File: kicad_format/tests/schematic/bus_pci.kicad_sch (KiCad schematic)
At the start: 33 parts, among them U1 24C16, U11 S5933_PQ160

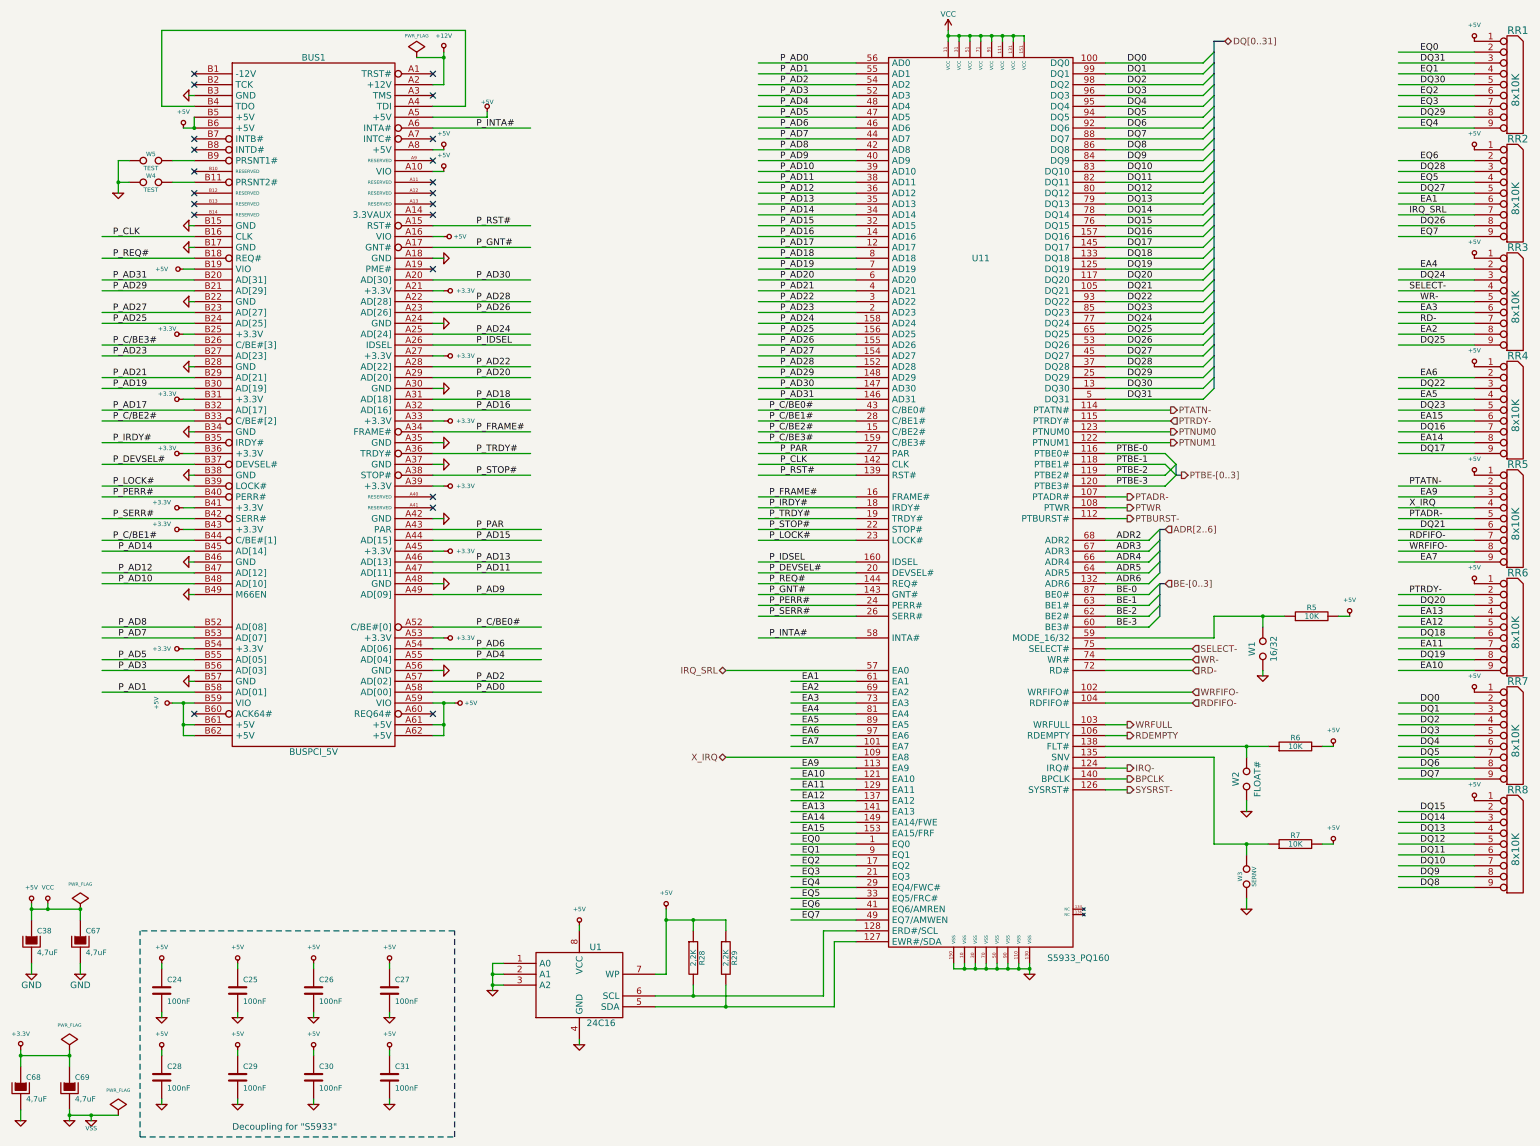
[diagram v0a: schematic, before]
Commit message: Add serialization context and support most modern kicad file idiosyncrasies
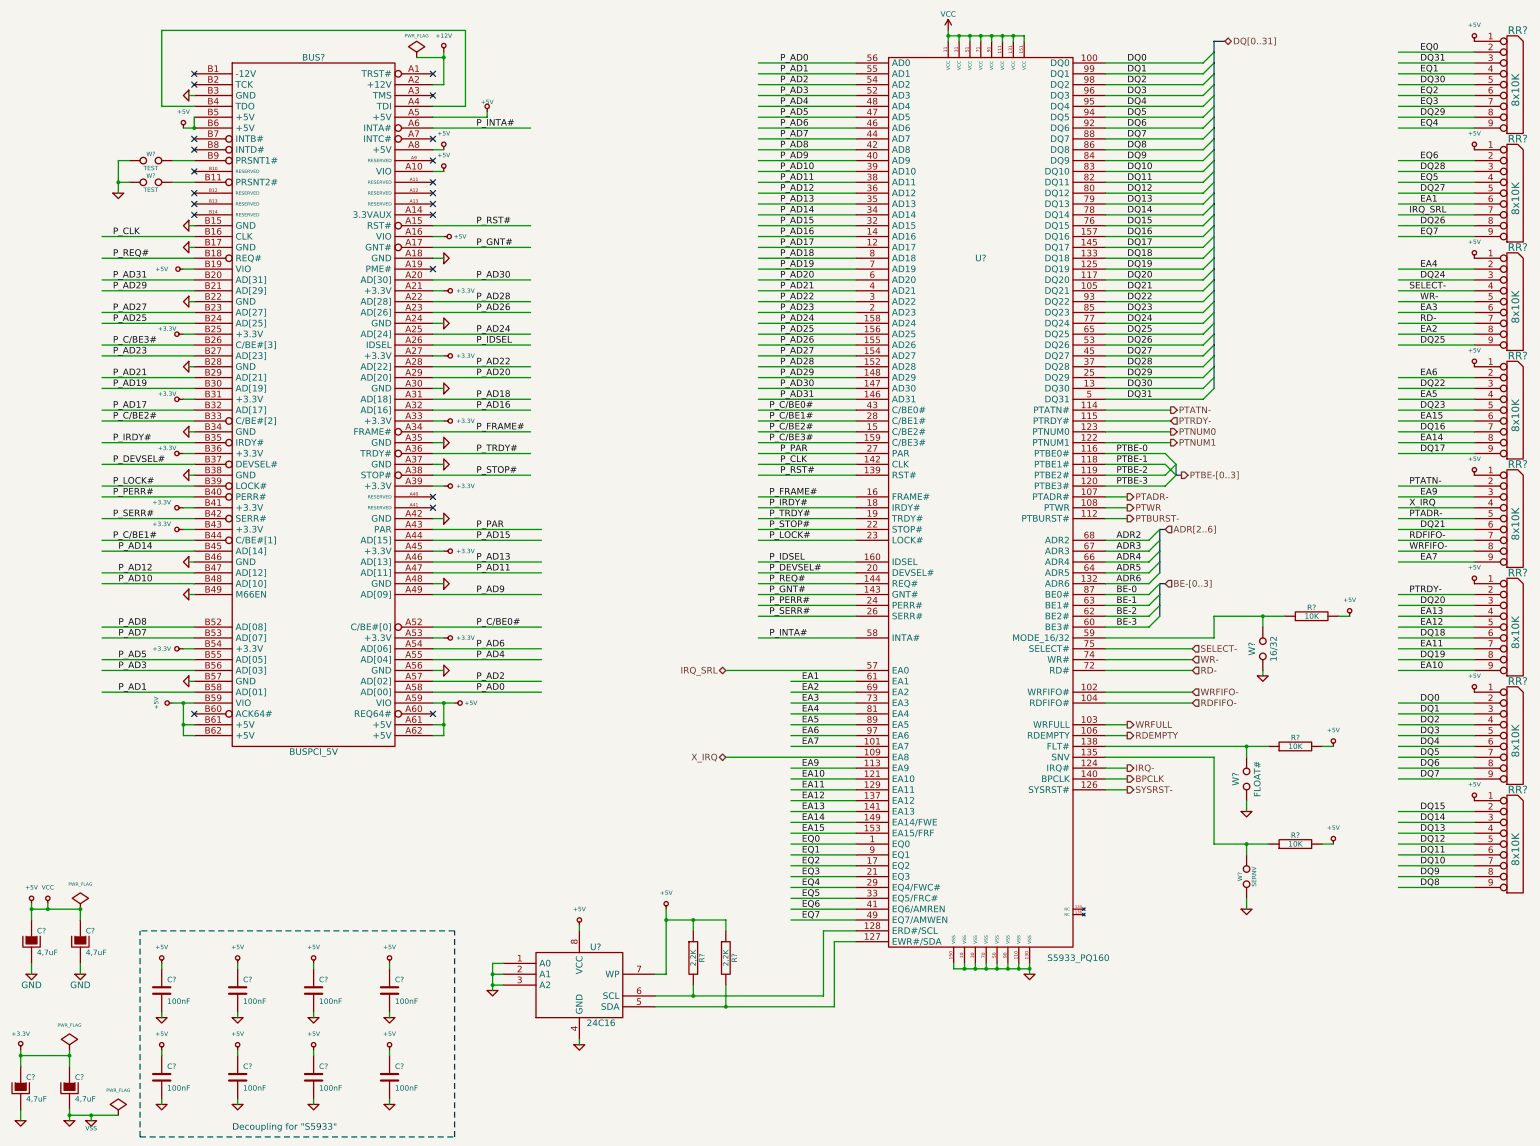
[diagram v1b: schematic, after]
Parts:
- renumbered BUS1 to BUS?, C24 to C?, C25 to C?, C26 to C?, C27 to C?, C28 to C?, C29 to C?, C30 to C?, C31 to C?, C38 to C?, C67 to C?, C69 to C?, C68 to C?, R5 to R?, R6 to R?, R7 to R?, R28 to R?, R29 to R?, RR7 to RR?, RR6 to RR?, RR4 to RR?, RR8 to RR?, RR3 to RR?, RR5 to RR?, RR2 to RR?, RR1 to RR?, U11 to U?, U1 to U?, W4 to W?, W5 to W?, W1 to W?, W2 to W?, W3 to W?
